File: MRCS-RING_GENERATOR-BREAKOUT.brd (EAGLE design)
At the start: 50 x 69 mm, 12 parts

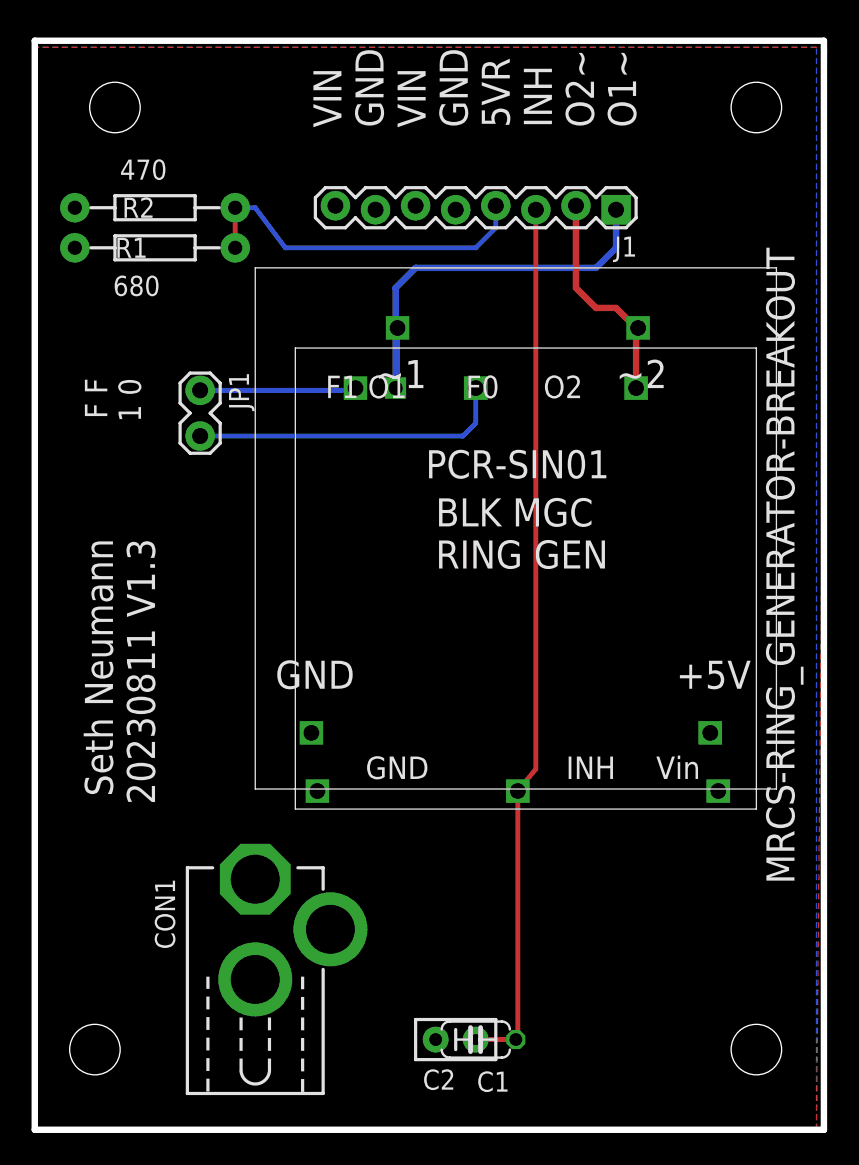
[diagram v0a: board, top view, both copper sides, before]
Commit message: panelized 2 up version
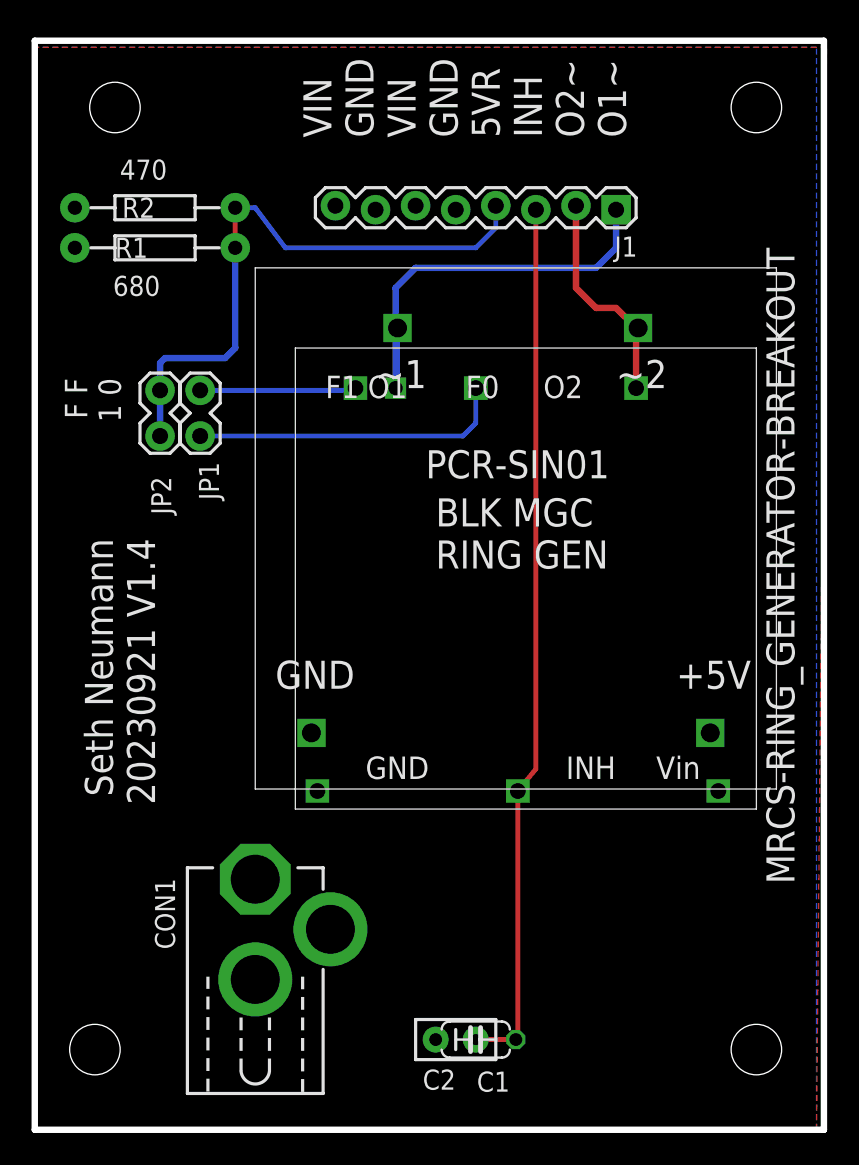
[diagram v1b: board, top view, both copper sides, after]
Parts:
- added JP2: (no value), SPCoast:1X02_LOCK
- moved U$3 19.1 mm to (25.4, 35.6)
- moved U$4 10.2 mm to (26.7, 12.7)
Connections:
- net 5VREF: now also JP2.1, JP2.2
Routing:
- net 5VREF: track 22.2 -> 38.4 mm
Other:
- board text added: "C1"
- board text added: "C2"
- board text added: "CON1"
- board text added: "J1"
- board text added: "JP1"
- board text added: "JP2"
- board text added: "R1"
- board text added: "R2"
- board text added: "Seth Neumann 20230921 V1.4"
- board text removed: "Seth Neumann 20230811 V1.3"
